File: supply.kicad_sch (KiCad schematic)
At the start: 23 parts, among them Q5 BC817-25W, U4 TLV70012_SC70, U5 TLV70033_SC70, U6 TLV70025_SC70

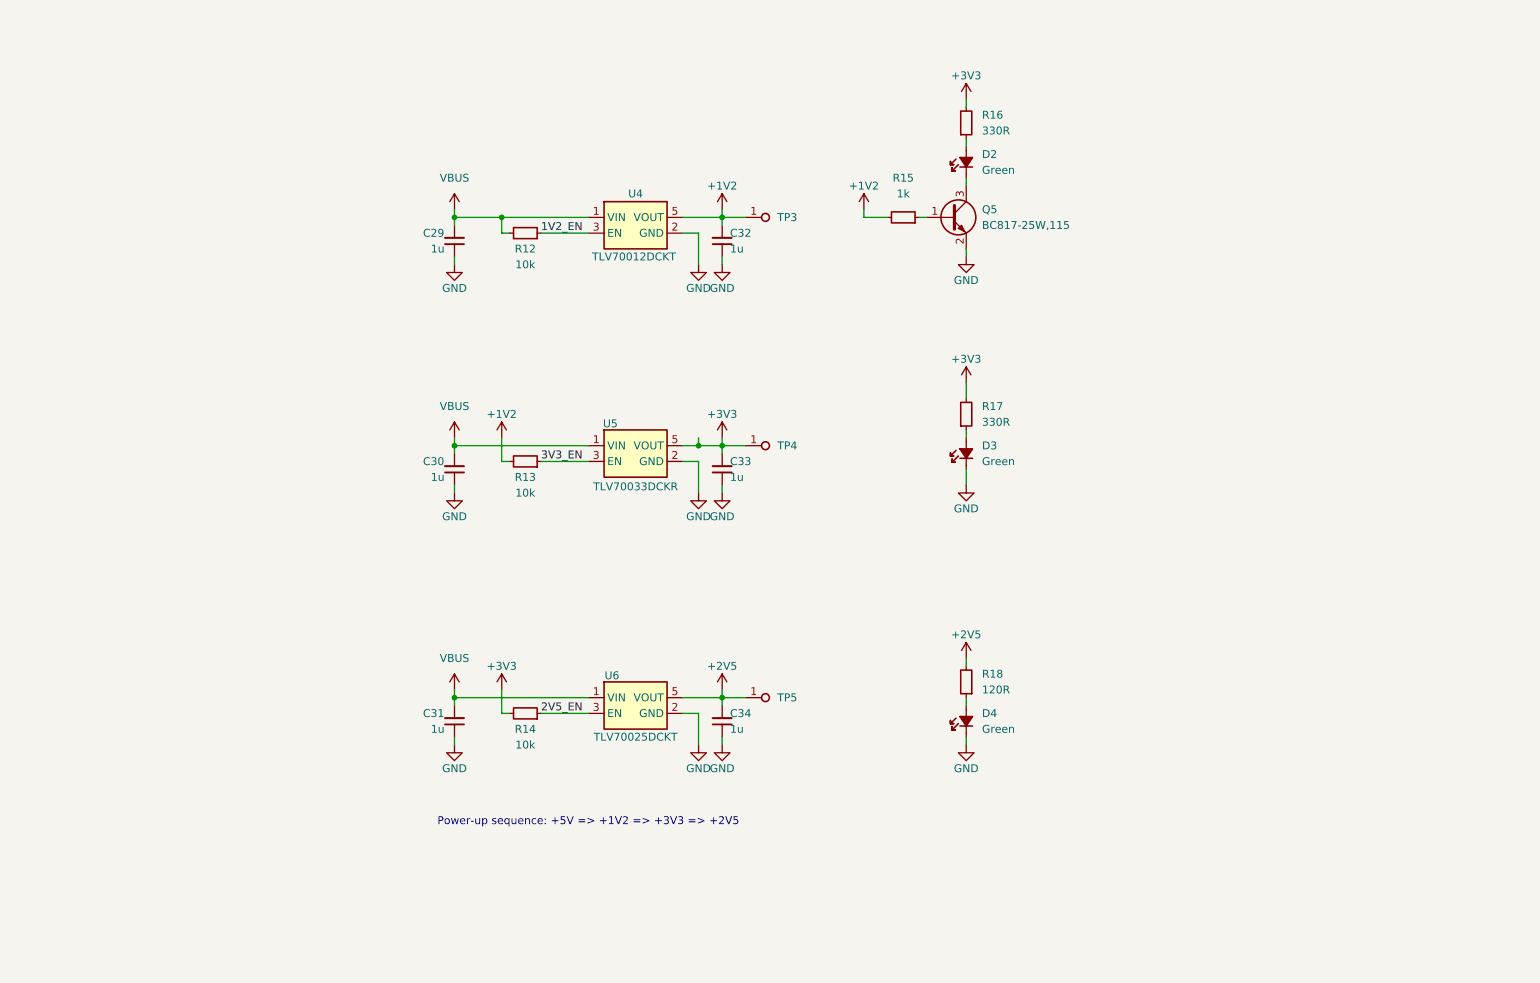
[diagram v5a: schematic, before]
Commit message: [#72133] Sch: Update power section
Signed-off-by: Dawid Lentka <dlentka@antmicro.com>
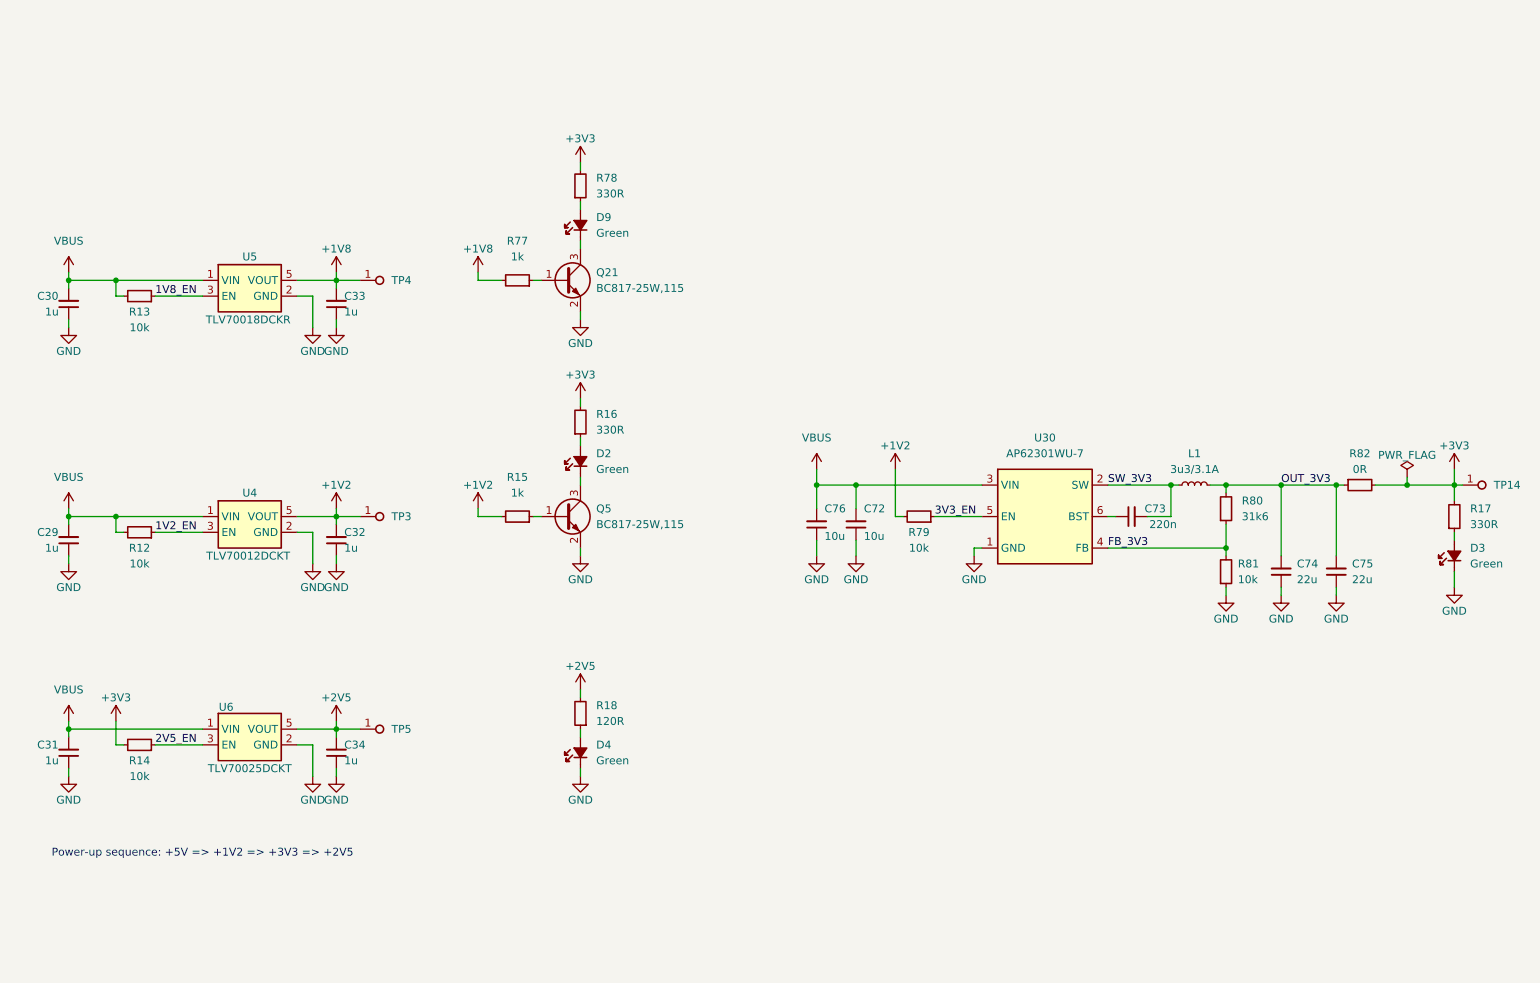
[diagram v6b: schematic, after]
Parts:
- removed U5: TLV70033_SC70, antmicro-footprints:SC-70-5, symbol antmicroPMICVoltageRegulatorsLinear:TLV70033_SC70
- added C72, C76: C_10u_0402, antmicro-footprints:C_0402_1005Metric, symbol antmicroCapacitors0402:C_10u_0402
- added C73: C_220n_0402, antmicro-footprints:C_0402_1005Metric, symbol antmicroCapacitors0402:C_220n_0402
- added C74, C75: C_22u_0402, antmicro-footprints:C_0402_1005Metric, symbol antmicroCapacitors0402:C_22u_0402
- added D9: LED_G_0603_KP-1608CGCK, antmicro-footprints:LED_0603_1608Metric_G, symbol antmicroLEDIndicationDiscrete:LED_G_0603_KP-1608CGCK
- added L1: L_3u3_3.1A_Bourns-SRP3212A, antmicro-footprints:L_Bourns-SRP3212A, symbol antmicroFixedInductors:L_3u3_3.1A_Bourns-SRP3212A
- added Q21: BC817-25W, antmicro-footprints:SOT-323, symbol antmicroTransistorsBipolarSingle:BC817-25W
- added R77: R_1k_0402, antmicro-footprints:R_0402_1005Metric, symbol antmicroResistors0402:R_1k_0402
- added R78: R_330R_0402, antmicro-footprints:R_0402_1005Metric, symbol antmicroResistors0402:R_330R_0402
- added R79, R81: R_10k_0402, antmicro-footprints:R_0402_1005Metric, symbol antmicroResistors0402:R_10k_0402
- added R80: R_31k6_0402, antmicro-footprints:R_0402_1005Metric, symbol antmicroResistors0402:R_31k6_0402
- added R82: R_0R_0402, antmicro-footprints:R_0402_1005Metric, symbol antmicroResistors0402:R_0R_0402
- added TP14: TP_1.5mm_SMD, antmicro-footprints:TP_SMD_1.5mm, symbol antmicroTestPoints:TP_1.5mm_SMD
- added U30: AP62301_TSOT, antmicro-footprints:TSOT23-6, symbol antmicroDCDCConverters:AP62301_TSOT
- added U5: TLV70018_SC70, antmicro-footprints:SC-70-5, symbol antmicroPMICVoltageRegulatorsLinear:TLV70018_SC70
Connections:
- net +1V2: now also R79.2; no longer R13.2
- net +3V3: now also R78.2, R82.2, TP14.1; no longer C33.2, TP4.1
- net 3V3_EN: now also R79.1, U30.5 (EN); no longer R13.1
- net GND: now also C72.1, C74.1, C75.1, C76.1, Q21.2 (E), R81.1, U30.1 (GND), U5.2 (GND)
- net VBUS: now also R13.2, C72.2, C76.2, U30.3 (VIN), U5.1 (VIN)
- new net: Q21.1 (B), R77.1
- new net: D9.1 (C), Q21.3 (C)
- new net: C73.1, U30.6 (BST)
- new net: D9.2 (A), R78.1
- new net +1V8: C33.2, R77.2, TP4.1, U5.5 (VOUT)
- new net 1V8_EN: R13.1, U5.3 (EN)
- new net FB_3V3: R80.1, R81.2, U30.4 (FB)
- new net OUT_3V3: C74.2, C75.2, L1.2, R80.2, R82.1
- new net SW_3V3: C73.2, L1.1, U30.2 (SW)
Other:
- moved on the sheet: C29, C31, C32, C34, D2, D3, D4, Q5, R12, R14, R15, R16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

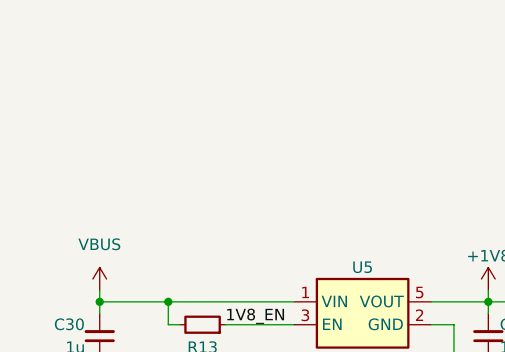
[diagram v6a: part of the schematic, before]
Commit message: [#72133] Sch: Update control hierarchy
Signed-off-by: Dawid Lentka <dlentka@antmicro.com>
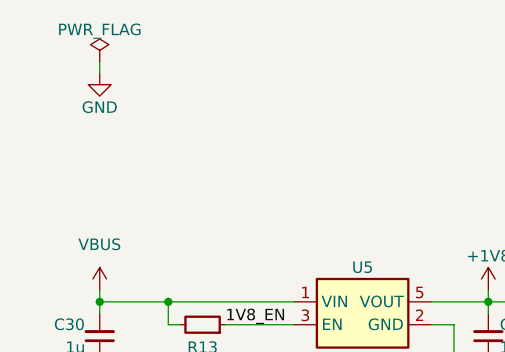
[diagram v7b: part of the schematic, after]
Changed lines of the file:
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@@
 	(wire
 		(pts
+			(xy 45.72 38.1) (xy 45.72 39.37)
+		)
+		(stroke
+			(width 0)
+			(type default)
+		)
+	)
+	(wire
+		(pts
 			(xy 213.36 102.87) (xy 214.63 102.87)
 		)
@@
 	)
 	(symbol
+		(lib_id "antmicropower:PWR_FLAG")
+		(at 45.72 38.1 0)
+		(unit 1)
+		(exclude_from_sim no)
+		(in_bom yes)
+		(on_board yes)
+		(dnp no)
+		(property "Reference" "#FLG02"
+			(at 45.72 36.195 0)
+			(effects
+				(font
+					(size 1.27 1.27)
+				)
+				(hide yes)
+			)
+		)
+		(property "Value" "PWR_FLAG"
+			(at 45.72 34.544 0)
+			(effects
+				(font
+					(size 1.27 1.27)
+				)
+			)
+		)
+		(property "Footprint" ""
+			(at 45.72 38.1 0)
+			(effects
+				(font
+					(size 1.27 1.27)
+				)
+				(hide yes)
+			)
+		)
+		(property "Datasheet" ""
+			(at 45.72 38.1 0)
+			(effects
+				(font
+					(size 1.27 1.27)
+				)
+				(hide yes)
+			)
+		)
+		(property "Description" ""
+			(at 45.72 38.1 0)
+			(effects
+				(font
+					(size 1.27 1.27)
+				)
+				(hide yes)
+			)
+		)
+		(pin "1"
+		)
+		(instances
+			(project "led-panel"
+				(path "/a86e1cab-ea0a-45e6-9194-d44b0d5c9450/558630aa-e7f2-4066-9d03-1c648a6adc39"
+					(reference "#FLG02")
+					(unit 1)
+				)
+			)
+		)
+	)
+	(symbol
 		(lib_id "antmicroTransistorsBipolarSingle:BC817-25W")
 		(at 121.92 64.77 0)
@@
 					(unit 1)
 				)
+			)
+		)
+	)
+	(symbol
+		(lib_id "antmicropower:GND")
+		(at 45.72 39.37 0)
+		(unit 1)
+		(exclude_from_sim no)
+		(in_bom yes)
+		(on_board yes)
+		(dnp no)
+		(property "Reference" "#PWR0123"
+			(at 54.61 41.91 0)
+			(effects
+				(font
+					(size 1.27 1.27)
+					(thickness 0.15)
+				)
+				(justify left bottom)
+				(hide yes)
+			)
+		)
+		(property "Value" "GND"
+			(at 45.72 43.18 0)
+			(effects
+				(font
+					(size 1.27 1.27)
+					(thickness 0.15)
+				)
+			)
+		)
+		(property "Footprint" ""
+			(at 54.61 46.99 0)
+			(effects
+				(font
+					(size 1.27 1.27)
+					(thickness 0.15)
+				)
+				(justify left bottom)
+				(hide yes)
+			)
+		)
+		(property "Datasheet" ""
+			(at 54.61 52.07 0)
+			(effects
+				(font
+					(size 1.27 1.27)
+					(thickness 0.15)
+				)
+				(justify left bottom)
+				(hide yes)
+			)
+		)
+		(property "Description" ""
+			(at 45.72 39.37 0)
+			(effects
+				(font
+					(size 1.27 1.27)
+				)
+				(hide yes)
+			)
+		)
+		(property "Author" "Antmicro"
+			(at 54.61 46.99 0)
+			(effects
+				(font
+					(size 1.27 1.27)
+					(thickness 0.15)
+				)
+				(justify left bottom)
+				(hide yes)
+			)
+		)
+		(property "License" "Apache-2.0"
+			(at 54.61 49.53 0)
+			(effects
+				(font
+					(size 1.27 1.27)
+					(thickness 0.15)
+				)
+				(justify left bottom)
+				(hide yes)
+			)
+		)
+		(pin "1"
+		)
+		(instances
+			(project "led-panel"
+				(path "/a86e1cab-ea0a-45e6-9194-d44b0d5c9450/558630aa-e7f2-4066-9d03-1c648a6adc39"
+					(reference "#PWR0123")
+					(unit 1)
+				)

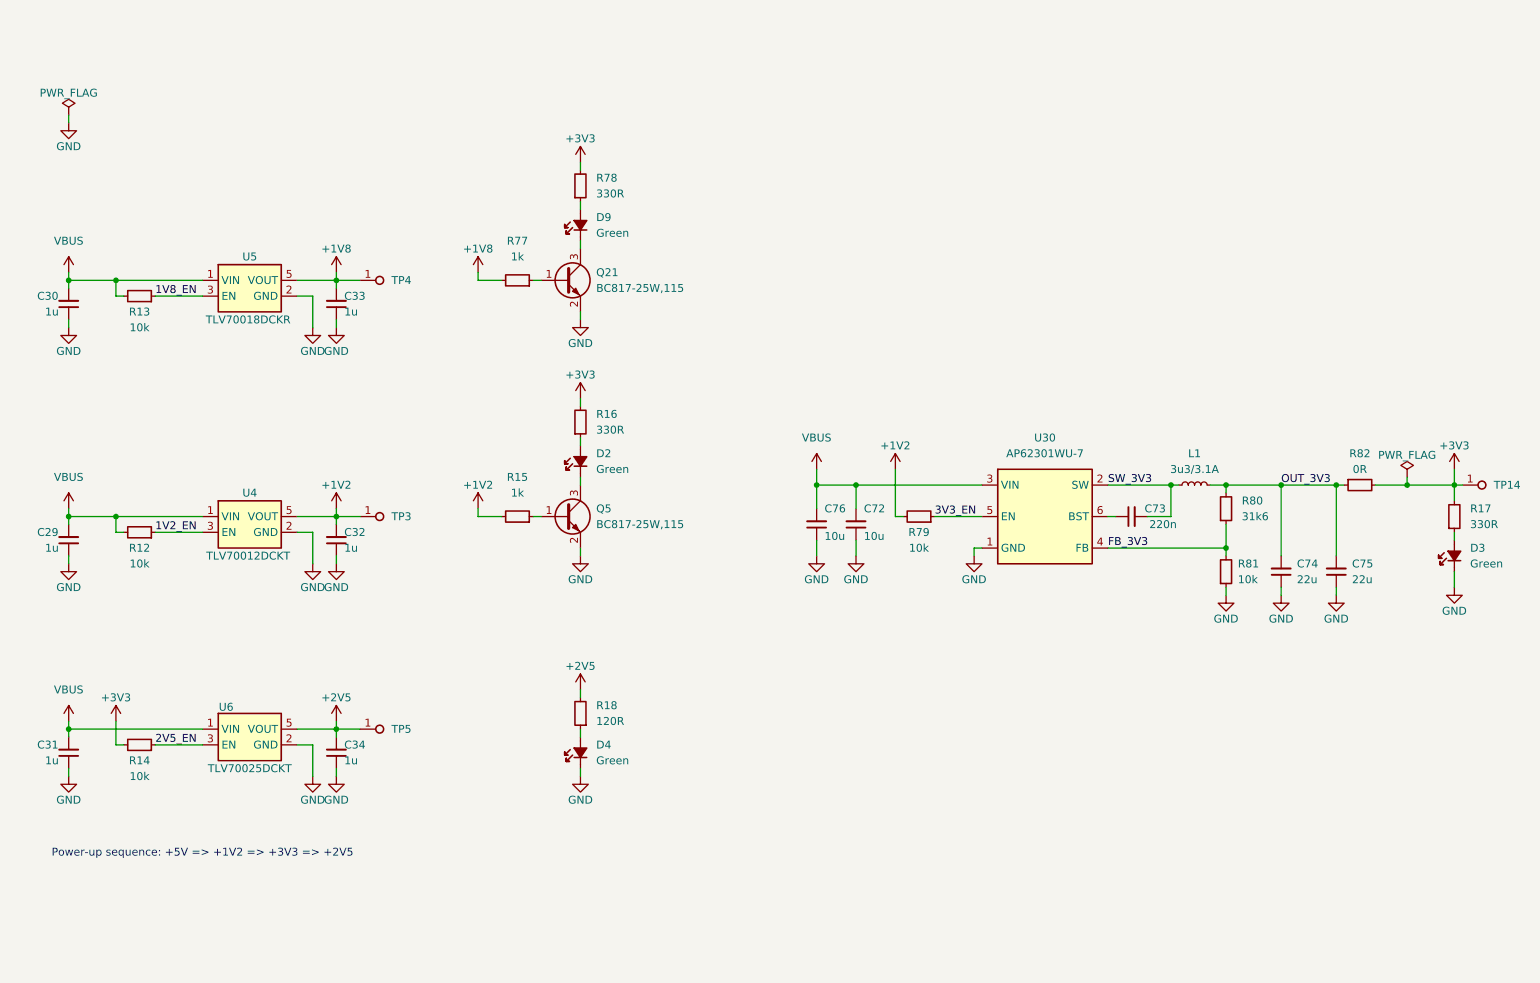
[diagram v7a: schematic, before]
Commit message: [#72133] Update supply schematic
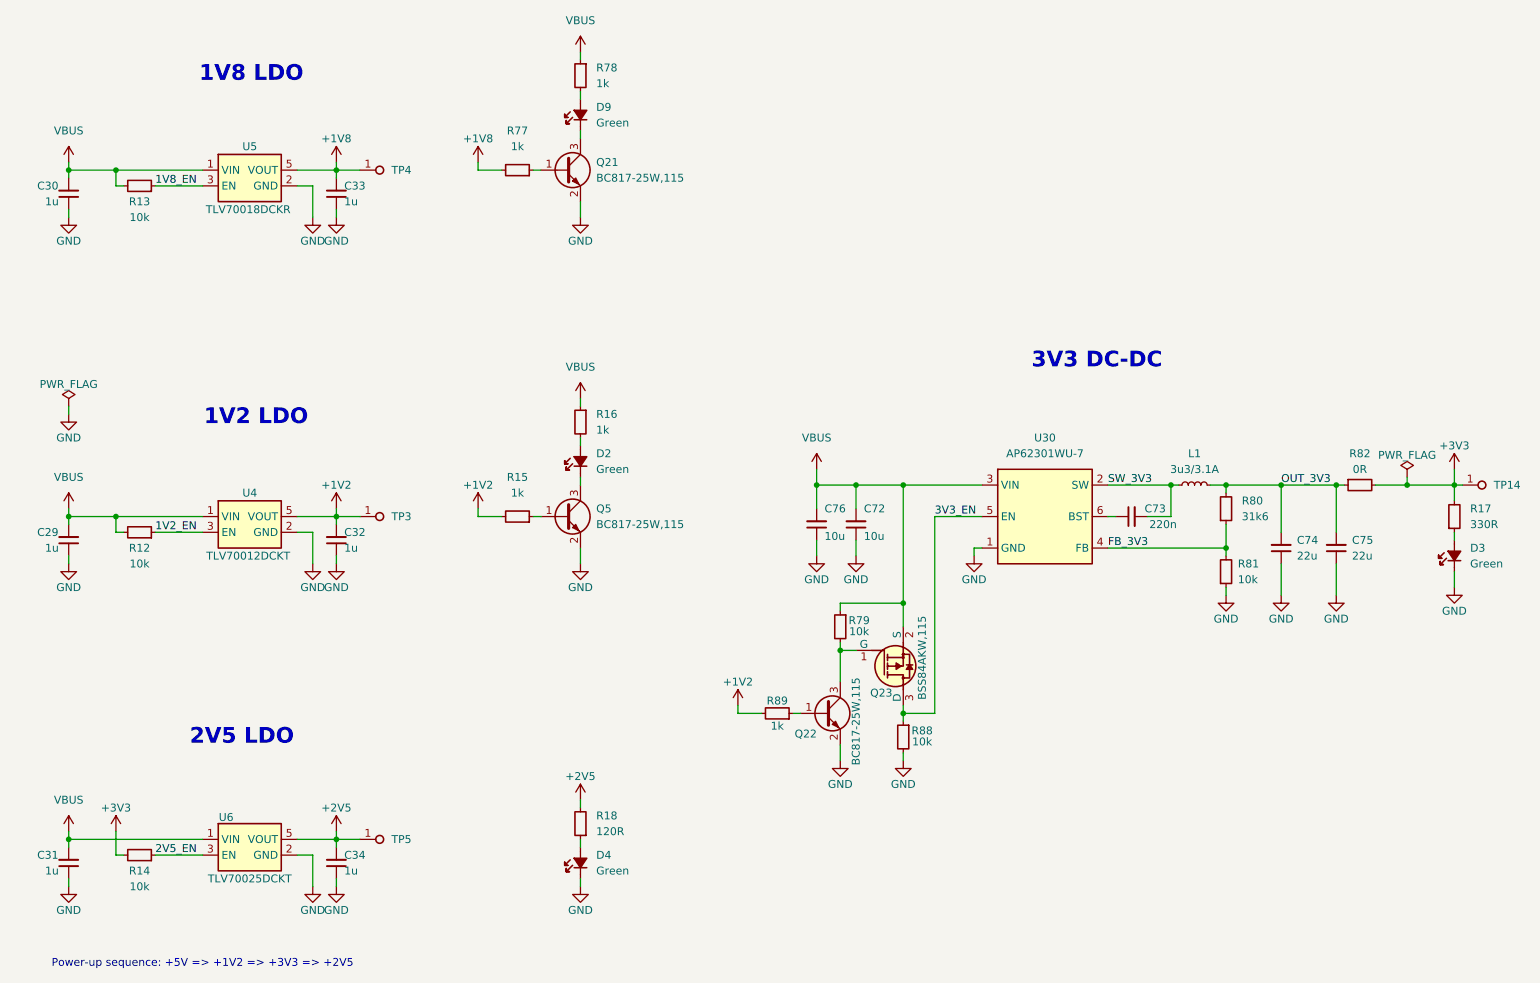
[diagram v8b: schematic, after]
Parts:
- removed R16, R78: R_330R_0402, antmicro-footprints:R_0402_1005Metric, symbol antmicroResistors0402:R_330R_0402
- removed TP14: TP_1.5mm_SMD, antmicro-footprints:TP_SMD_1.5mm, symbol antmicroTestPoints:TP_1.5mm_SMD
- added Q22: BC817-25W, antmicro-footprints:SOT-323, symbol antmicroTransistorsBipolarSingle:BC817-25W
- added Q23: BSS84AKW, antmicro-footprints:SOT-323, symbol antmicroTransistorsFETsMOSFETsSingle:BSS84AKW
- added R16, R78, R89: R_1k_0402, antmicro-footprints:R_0402_1005Metric, symbol antmicroResistors0402:R_1k_0402
- added R88: R_10k_0402, antmicro-footprints:R_0402_1005Metric, symbol antmicroResistors0402:R_10k_0402
- added TP14: TP_0.75mm_SMD, antmicro-footprints:TP_SMD_0.75mm, symbol antmicroTestPoints:TP_0.75mm_SMD
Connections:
- net +1V2: now also R89.2; no longer R79.2
- net +3V3: now also TP14.1
- net 3V3_EN: now also Q23.3 (D), R88.1; no longer R79.1
- net GND: now also Q22.2 (E), R88.2
- net VBUS: now also R79.1, Q23.2 (S), R16.1, R78.1
- net at D2.2 (A): now also R16.2
- net at D9.2 (A): now also R78.2
- new net: Q22.3 (C), Q23.1 (G), R79.2
- new net: Q22.1 (B), R89.1
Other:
- note added: "1V2 LDO"
- note added: "1V8 LDO"
- note added: "2V5 LDO"
- note added: "3V3 DC-DC"
- moved on the sheet: C30, C31, C33, C34, C74, C75, D4, D9, Q21, R13, R14, R18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
